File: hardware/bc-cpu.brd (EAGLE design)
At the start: 100 x 80 mm, 84 parts, among them J1 BATTERIES, J2 PHT, J3 LED Matrix, J4 12V, J5 5V, U1 R-735.0P, U2 MAX11632EEG+, U3 MAX11632EEG+, U4 AD1584BRTZ

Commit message: Rough placement, no routes
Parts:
- moved R65 174.0 mm to (82.5, 76.2)
- moved R63 140.7 mm to (36.8, 34.3)
- moved R64 139.7 mm to (30.5, 34.3)
- moved R35 135.3 mm to (36.8, 52.1)
- moved R47 127.9 mm to (36.8, 44.5)
- moved R48 126.8 mm to (30.5, 44.5)
- moved R49 126.1 mm to (22.9, 41.9)
- moved R50 125.1 mm to (16.5, 41.9)
- moved R19 124.9 mm to (36.8, 62.2)
- moved R20 123.7 mm to (30.5, 62.2)
- moved R59 123.3 mm to (36.8, 36.8)
- moved R60 122.3 mm to (30.5, 36.8)
- moved R61 122.2 mm to (22.9, 34.3)
- moved R62 121.3 mm to (16.5, 34.3)
- moved R31 115.9 mm to (36.8, 54.6)
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
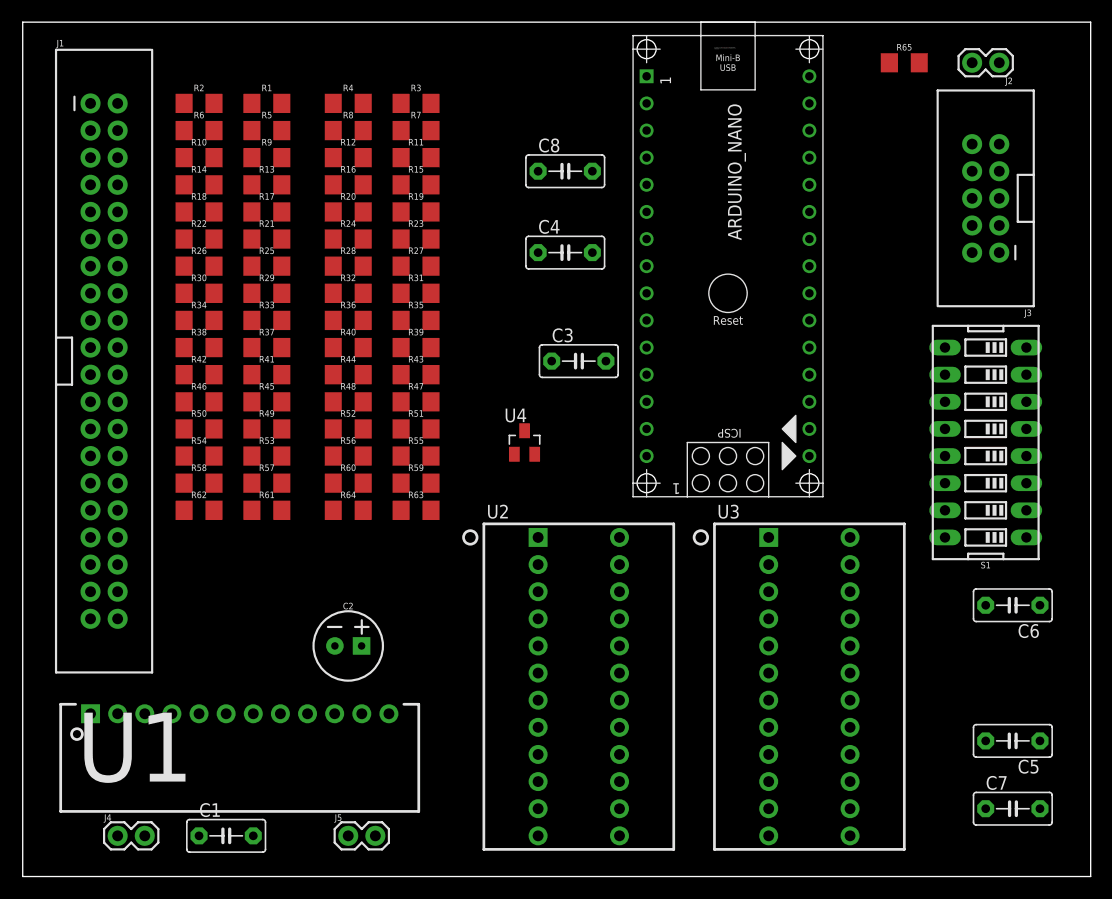
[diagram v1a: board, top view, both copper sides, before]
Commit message: Layout attempt with SMD MAX-11632
Lots of random traces that need to be placed by hand. Committing before
trying a different approach.
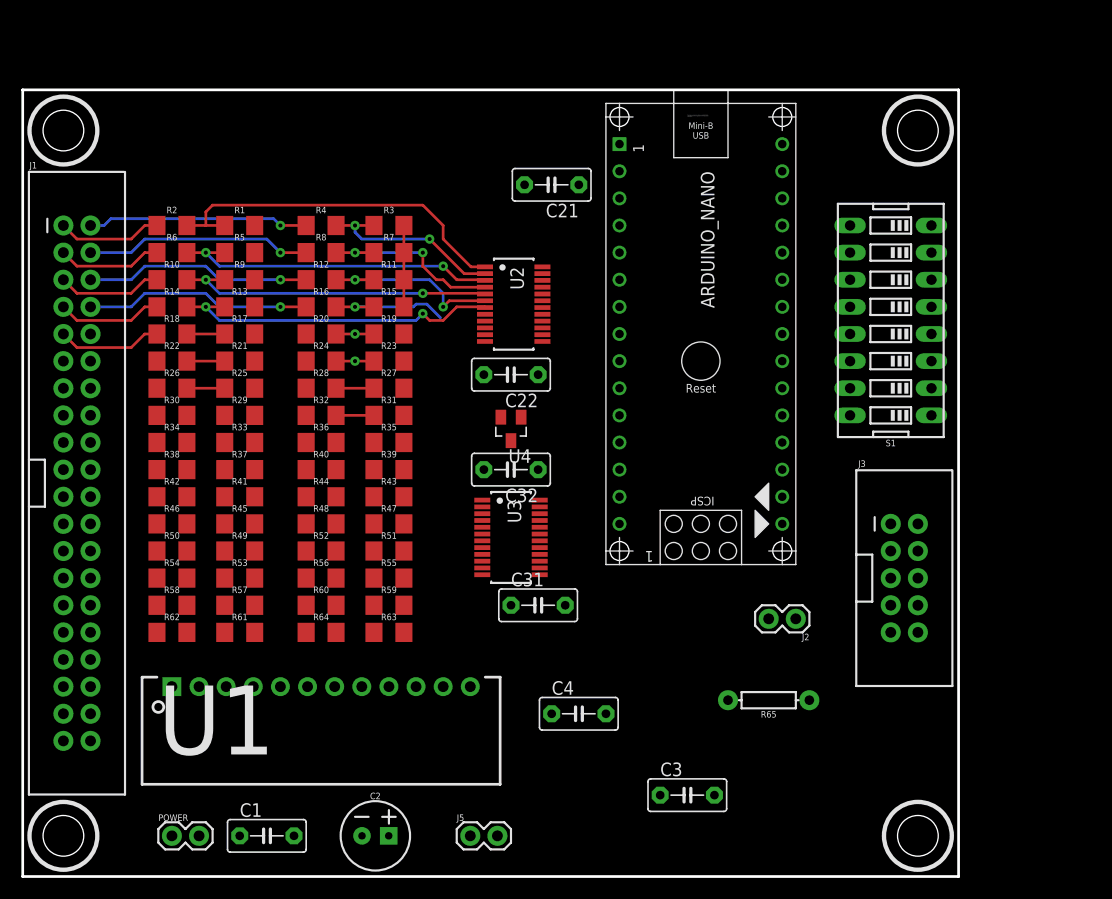
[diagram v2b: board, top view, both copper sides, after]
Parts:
- removed C5, C6, C7, C8: 0.1uF, capacitor-wima:C5B3
- removed J4: 12V, SparkFun-Connectors:1X02
- added C21, C22, C31, C32: 0.1uF, capacitor-wima:C5B3
- added POWER: 12V, SparkFun-Connectors:1X02
- J5: value 5V -> BRK5
- R65: value 10K -> (none); device SparkFun-Resistors:1206 -> SparkFun-Resistors:AXIAL-0.3
- U2, U3: device MAX-11632:ADPT24 -> MAX-11632:QSOP24
- moved R65 61.0 mm to (69.8, 16.5), turned to 180 degrees
- moved J2 55.4 mm to (72.4, 24.1)
- moved C4 43.2 mm to (52.1, 15.2)
- moved C3 41.9 mm to (62.2, 7.62)
- moved J3 36.4 mm to (82.5, 27.9), turned to 0 degrees
- moved U2 35.1 mm to (46.0, 53.6), turned to 270 degrees
- moved U3 30.7 mm to (45.7, 31.8), turned to 270 degrees
- moved C2 18.0 mm to (33.0, 3.81)
- moved S1 14.5 mm to (81.3, 52.1)
- moved J1 11.7 mm to (5.08, 36.8)
- moved R1 11.7 mm to (20.3, 61.0)
- moved R10 11.7 mm to (14.0, 55.9)
- moved R11 11.7 mm to (34.3, 55.9)
- moved R12 11.7 mm to (27.9, 55.9)
- moved R17 11.7 mm to (20.3, 50.8)
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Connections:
- removed net N$10: C1.1, J4.1, U1.2, U1.3, U1.4
- net GND: now also C21.2, C22.2, C31.2, C32.2, POWER.1, R65.P$2; no longer C5.2, C6.2, C7.2, C8.2, R65.2
- net N$2: now also C31.1; no longer C7.1
- net N$3: now also C21.1; no longer C8.1
- net PHOTO: now also R65.P$1; no longer R65.1
- net V5V: now also C22.1, C32.1; no longer C5.1, C6.1
- net VCC: now also C1.1, POWER.2, U1.2, U1.3, U1.4; no longer J4.2
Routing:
- net CV01: track 0.00 -> 34.4 mm
- net CV07: track 0.00 -> 31.3 mm, vias 0 -> 2
- net CV03: track 0.00 -> 30.8 mm, vias 0 -> 2
- net CV05: track 0.00 -> 30.2 mm, vias 0 -> 2
- net BV08: track 0.00 -> 21.2 mm, vias 0 -> 1
- net BV06: track 0.00 -> 21.2 mm, vias 0 -> 1
- net BV04: track 0.00 -> 21.2 mm, vias 0 -> 1
- net BV02: track 0.00 -> 20.7 mm, vias 0 -> 1
- net CV02: track 0.00 -> 18.0 mm, vias 0 -> 2
- net CV04: track 0.00 -> 17.8 mm, vias 0 -> 2
- net CV06: track 0.00 -> 17.8 mm, vias 0 -> 2
- net CV08: track 0.00 -> 12.2 mm, vias 0 -> 1
- net BV07: track 0.00 -> 9.81 mm
- net BV05: track 0.00 -> 9.81 mm
- net BV03: track 0.00 -> 9.81 mm
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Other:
- board size 100 x 80 mm -> 87.6 x 73.7 mm

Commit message: More organized routing
This starts to look like it might work... :)
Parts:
- moved C22 2.84 mm to (48.3, 45.7)
- moved U2 1.27 mm to (47.2, 53.6)
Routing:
- net GND: track 7.62 -> 74.6 mm
- net CV09: track 3.55 -> 32.5 mm, vias 0 -> 2
- net BV30: track 0.00 -> 21.2 mm, vias 0 -> 1
- net BV16: track 0.00 -> 21.2 mm, vias 0 -> 1
- net BV14: track 0.00 -> 21.2 mm, vias 0 -> 1
- net BV12: track 0.00 -> 21.2 mm, vias 0 -> 1
- net BV10: track 0.00 -> 21.2 mm, vias 0 -> 1
- net BV32: track 0.00 -> 21.2 mm, vias 0 -> 1
- net BV28: track 0.00 -> 21.2 mm, vias 0 -> 1
- net BV26: track 0.00 -> 21.2 mm, vias 0 -> 1
- net BV24: track 0.00 -> 21.2 mm, vias 0 -> 1
- net BV22: track 0.00 -> 21.2 mm, vias 0 -> 1
- net BV20: track 0.00 -> 21.2 mm, vias 0 -> 1
- net BV18: track 0.00 -> 21.2 mm, vias 0 -> 1
- net CV16: track 3.55 -> 23.4 mm, vias 0 -> 1
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
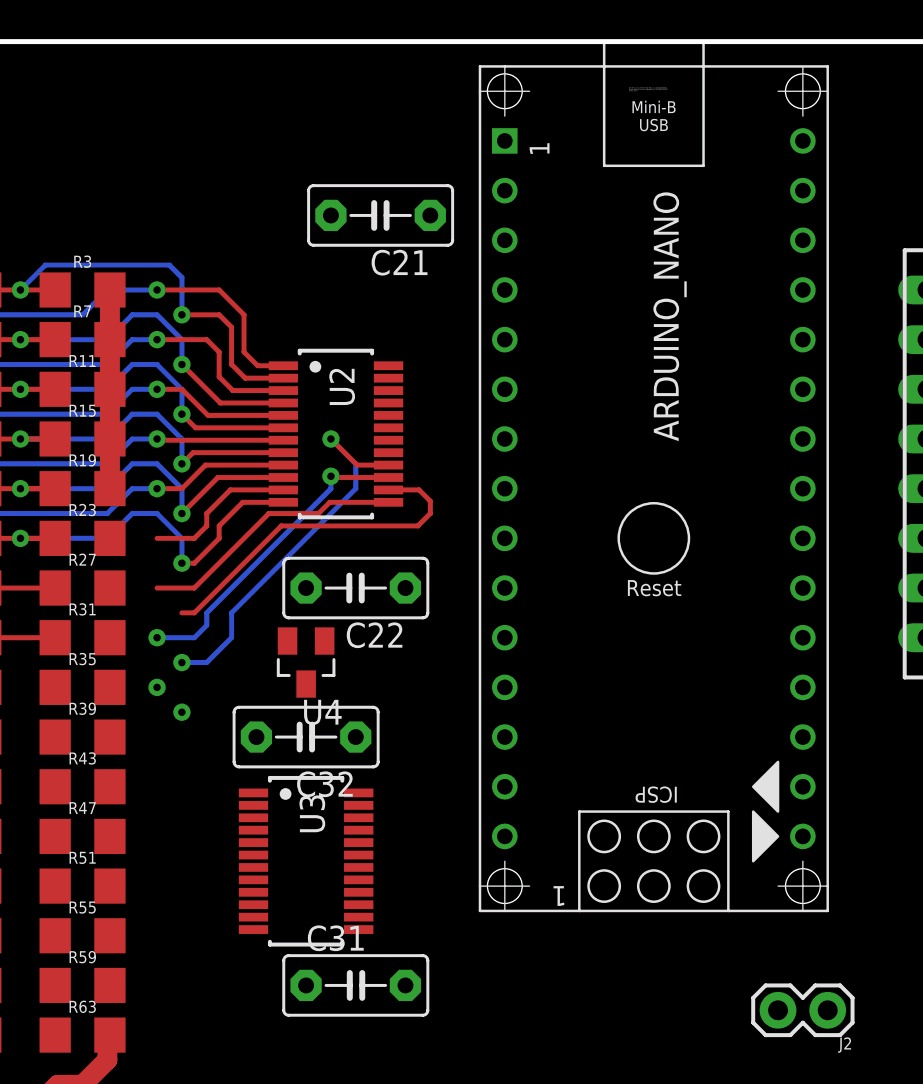
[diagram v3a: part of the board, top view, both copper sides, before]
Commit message: ADC 1 mostly routed
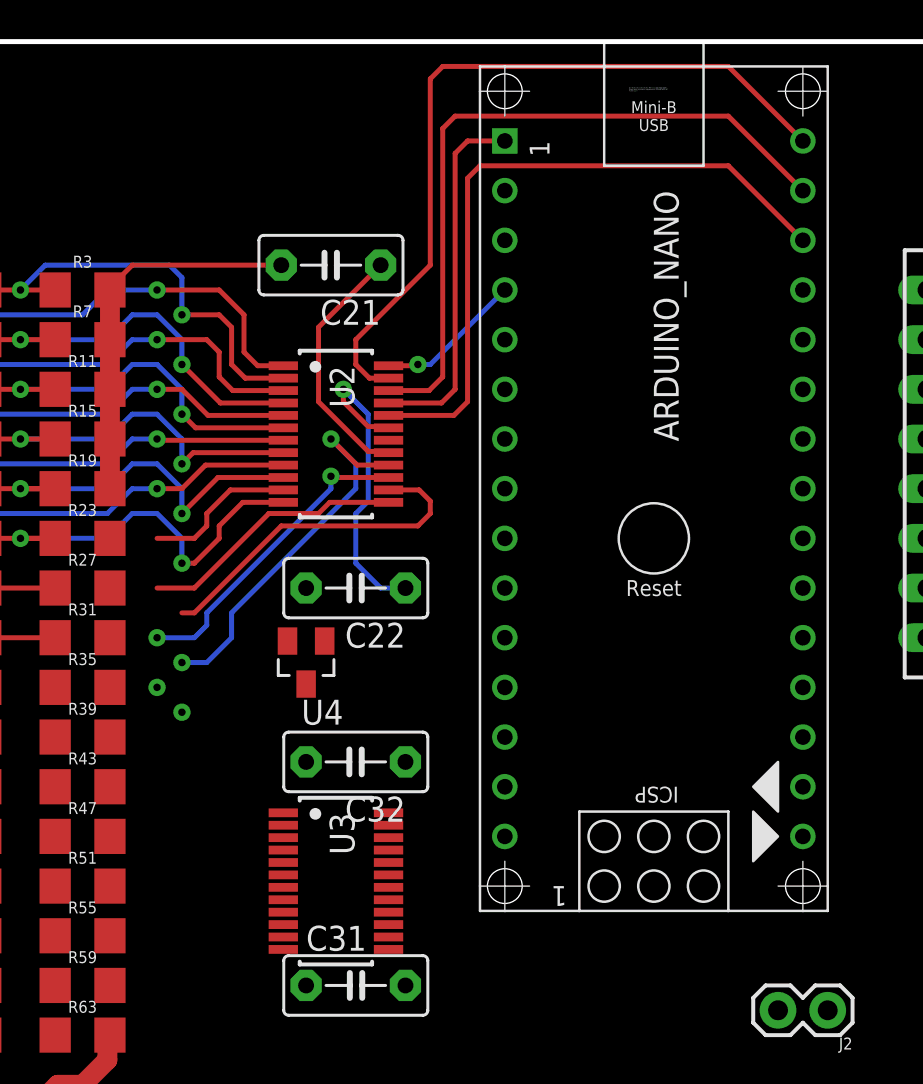
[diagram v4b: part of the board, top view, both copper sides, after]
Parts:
- moved C21 3.59 mm to (47.0, 62.2)
- moved C32 2.84 mm to (48.3, 36.8)
- moved U3 1.83 mm to (47.2, 30.7)
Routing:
- net MISO: track 0.00 -> 39.0 mm
- net MOSI: track 0.00 -> 36.0 mm
- net CS0: track 0.00 -> 34.7 mm
- net SCLK: track 0.00 -> 18.6 mm
- net V5V: track 0.00 -> 16.2 mm, vias 0 -> 1
- net N$3: track 0.00 -> 13.0 mm
- net GND: track 74.6 -> 83.1 mm
- net EOC0: track 0.00 -> 7.55 mm, vias 0 -> 1
- net CV16: vias 1 -> 2
- net CV15: vias 1 -> 2

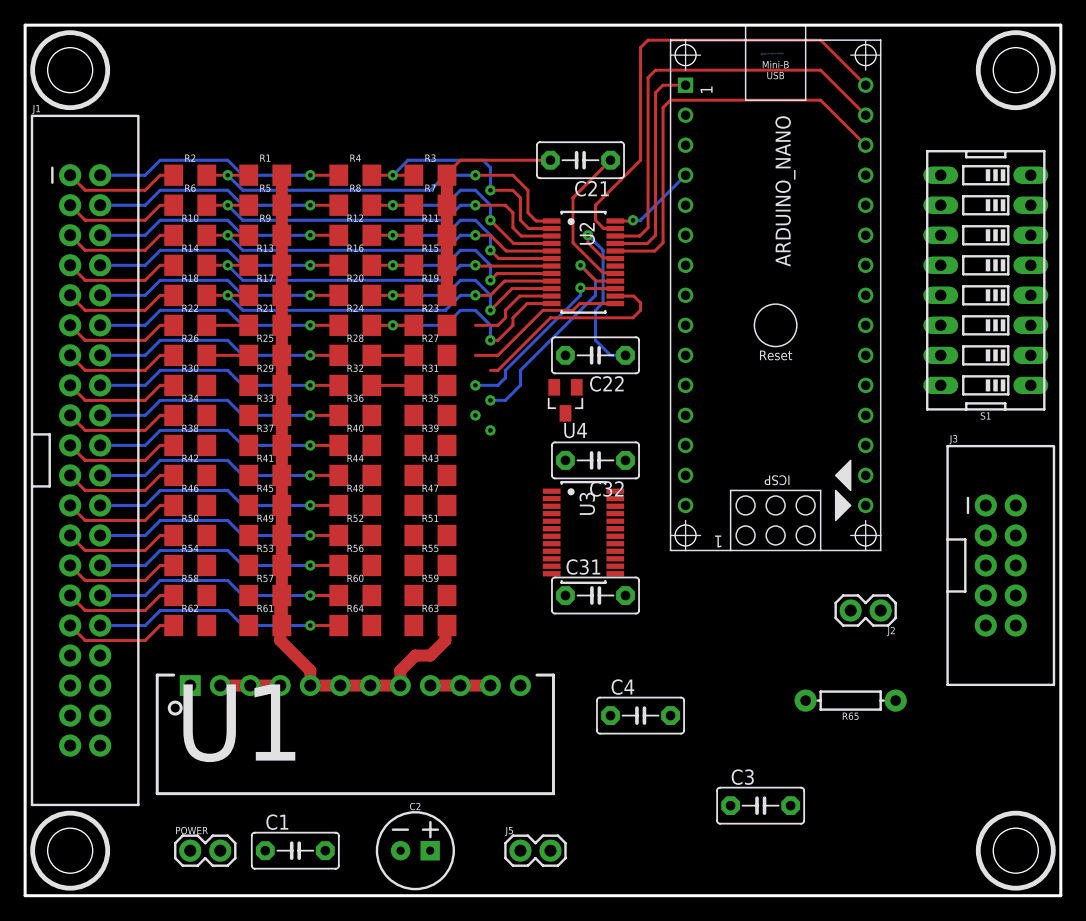
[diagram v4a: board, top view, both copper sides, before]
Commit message: Fixed VREF bug, mostly routed
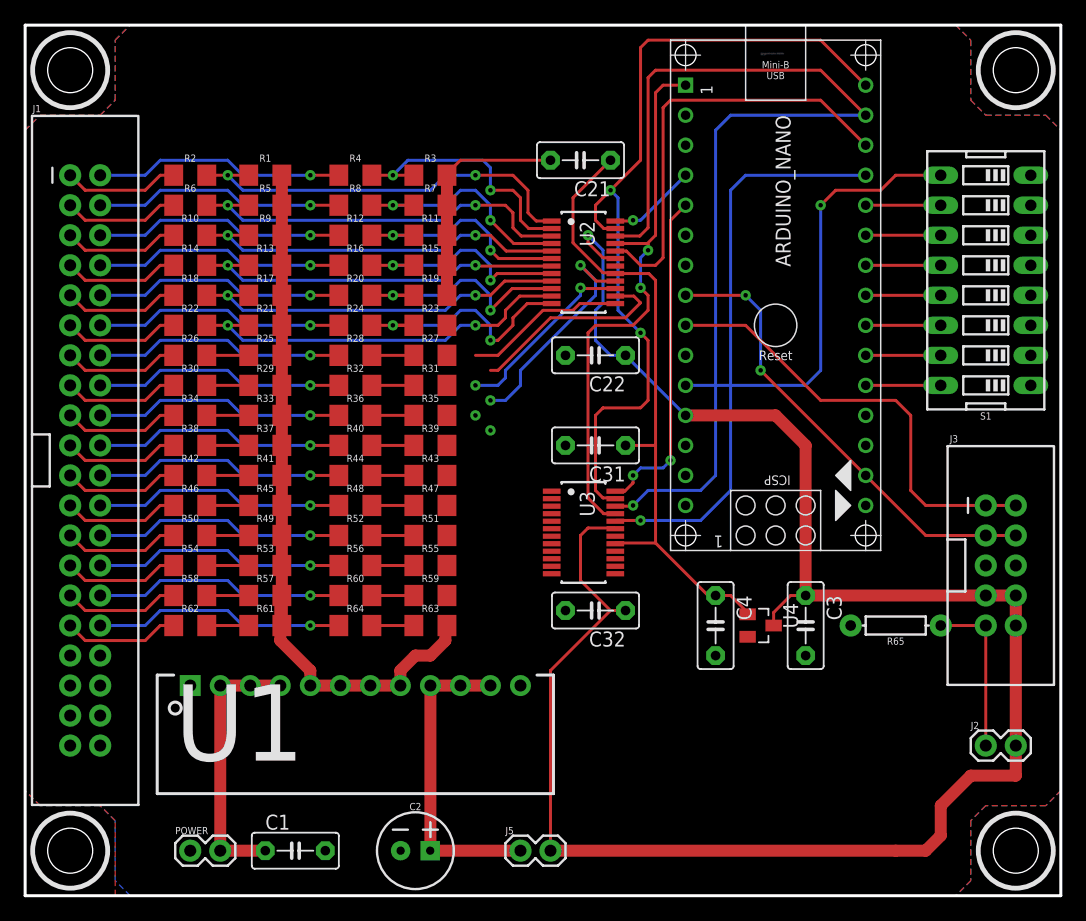
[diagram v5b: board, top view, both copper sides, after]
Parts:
- moved U4 25.2 mm to (62.2, 22.9), turned to 270 degrees
- moved C3 15.7 mm to (66.0, 22.9), turned to 270 degrees
- moved J2 14.5 mm to (81.3, 12.7), turned to 0 degrees
- moved C31 12.7 mm to (48.3, 38.1), turned to 180 degrees
- moved C32 12.7 mm to (48.3, 24.1)
- moved C4 9.92 mm to (58.4, 22.9), turned to 270 degrees
- moved R65 7.41 mm to (73.7, 22.9)
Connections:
- removed net N$2: C31.1, U3.17
- removed net N$3: C21.1, U2.17
- net VREF: now also C21.1, C31.1, U2.17, U3.17
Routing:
- net V5V: track 16.2 -> 162.6 mm
- net VREF: track 0.00 -> 55.2 mm
- net MOSI: track 36.0 -> 88.0 mm, vias 0 -> 1
- net CS1: track 0.00 -> 48.2 mm, vias 0 -> 1
- net LEDDAT: track 0.00 -> 39.3 mm, vias 0 -> 2
- net LEDCLK: track 0.00 -> 38.0 mm
- net DIP8: track 0.00 -> 37.1 mm, vias 0 -> 1
- net MISO: track 39.0 -> 71.4 mm, vias 0 -> 2
- net SCLK: track 18.6 -> 47.5 mm, vias 0 -> 2
- net EOC1: track 0.00 -> 28.2 mm, vias 0 -> 2
- net CV11: track 11.4 -> 33.4 mm, vias 0 -> 2
- net N$11: track 5.08 -> 26.7 mm
- net VCC: track 5.08 -> 22.9 mm
- net PHOTO: track 0.00 -> 14.0 mm
- net N$3: track 13.0 -> 0.00 mm
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- added copper zone on layer 1, net GND
- added copper zone on layer 16, net GND

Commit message: All routed, DRC checks passing
Also removed drill holes from Arduino Nano lib -- they were translating
into the board for no reason. Replaced them with just silkscreen.
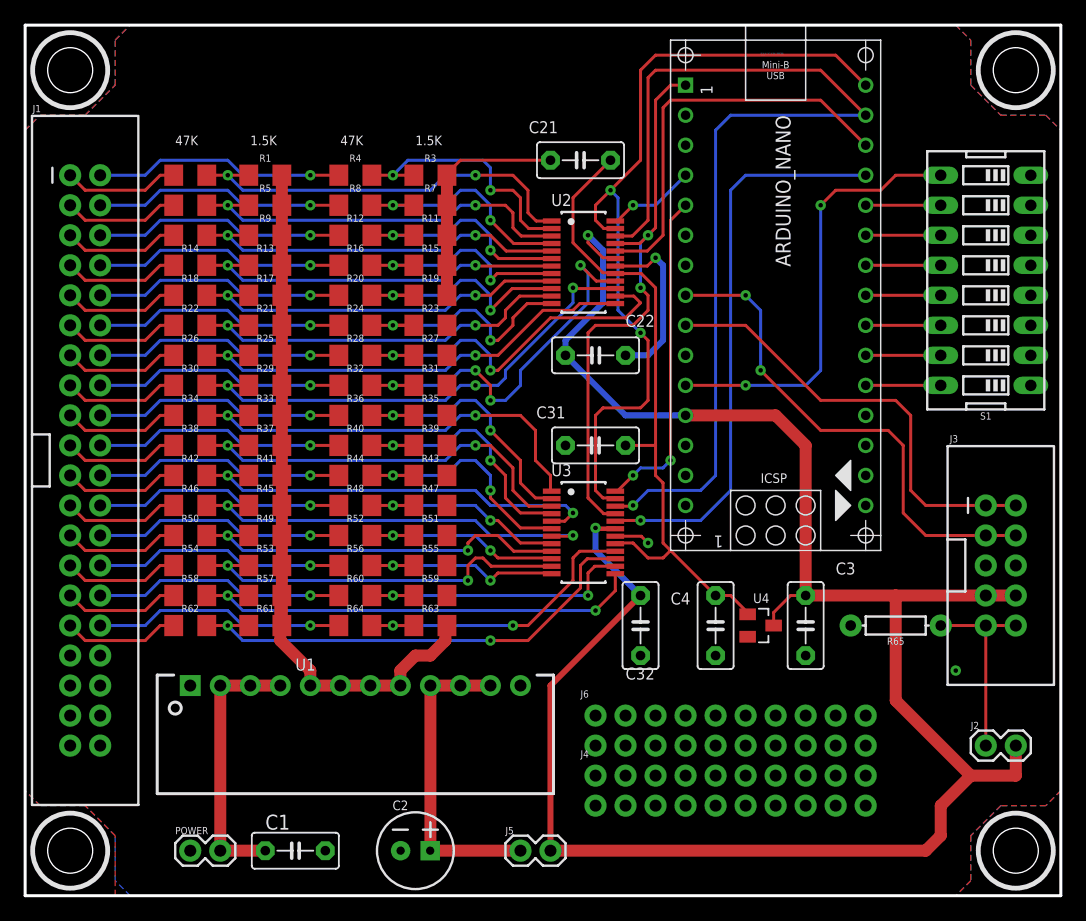
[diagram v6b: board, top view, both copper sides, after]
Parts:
- added J4, J6: (no value), SparkFun-Connectors:2X10_NOSILK
- moved C32 4.02 mm to (52.1, 22.9), turned to 270 degrees
- turned C22 to 0 degrees
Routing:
- net CV31: track 3.55 -> 40.8 mm, vias 0 -> 2
- net CV29: track 3.55 -> 39.0 mm, vias 0 -> 2
- net CV17: track 3.55 -> 36.9 mm, vias 0 -> 2
- net CV21: track 3.55 -> 36.2 mm, vias 0 -> 2
- net CV23: track 3.55 -> 35.6 mm, vias 0 -> 2
- net CV19: track 3.55 -> 35.3 mm, vias 0 -> 2
- net CV27: track 3.55 -> 33.3 mm, vias 0 -> 2
- net CV25: track 3.55 -> 32.9 mm, vias 0 -> 2
- net CV32: track 3.55 -> 26.1 mm, vias 0 -> 2
- net CV15: track 19.6 -> 42.0 mm, vias 2 -> 3
- net CV13: track 17.2 -> 39.2 mm, vias 0 -> 2
- net CV30: track 3.55 -> 24.5 mm, vias 0 -> 2
- net CV18: track 3.55 -> 22.8 mm, vias 0 -> 2
- net CV20: track 3.55 -> 22.3 mm, vias 0 -> 2
- net GND: track 83.1 -> 100.8 mm, vias 0 -> 3
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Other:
- board text added: "1.5K"
- board text added: "47K"
